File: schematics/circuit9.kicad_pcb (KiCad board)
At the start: 2 copper layers, 47.6 x 31.3 mm, 24 parts, among them J1 Right Pin Strip, J2 Left Pin Strip, J3 Pass-through Output Pin Strip, SW1 SW_DPST_x2, U1 TPS61220DCK, U2 LM321

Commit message: update circuits & order
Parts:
- added JP3: Solder Jumper, Jumper:SolderJumper-2_P1.3mm_Open_RoundedPad1.0x1.5mm, B.Cu at (61.3, 40.0)
- J1: value Right Pin Strip -> Left Pin Strip
- J2: value Left Pin Strip -> Right Pin Strip
- J3: value Pass-through Output Pin Strip -> I/O Pin Strip
- moved C7 9.15 mm to (63.8, 43.7)
- moved R4 6.80 mm to (54.7, 40.4), turned to 180 degrees
- moved R3 2.37 mm to (58.7, 40.4), turned to 180 degrees
- moved C1 2.29 mm to (28.5, 41.9)
- moved C2 2.29 mm to (30.8, 41.9)
- moved U2 1.65 mm to (58.5, 44.7)
- moved R1 0.63 mm to (33.8, 46.7)
- moved R2 0.63 mm to (33.8, 44.6)
- moved C3 0.38 mm to (37.3, 41.7)
- moved C4 0.38 mm to (39.6, 41.7)
- moved C5 0.38 mm to (41.9, 41.7)
- moved C6 0.38 mm to (44.1, 41.7)
- turned C10 to 90 degrees
- turned JP2 to 270 degrees
- renumbered C2 to C1, C1 to C2
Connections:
- C7 pad 1: /V+ -> Net-(C7-Pad1)
- JP2 pad 1: /A7 -> /Vbat
- JP2 pad 2: /Vbat -> /A7
- R3 pad 1: /V+ -> Net-(C7-Pad1)
- U2 pad 5: /V+ -> Net-(C7-Pad1)
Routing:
- net /Vbat: track 16.6 -> 37.3 mm, vias 2 -> 3
- net /GND: track 38.6 -> 18.6 mm, vias 10 -> 12
- net Net-(BT1-Pad1): track 9.16 -> 0.00 mm
- net /V+: track 90.0 -> 85.7 mm, vias 2 -> 4
- net Net-(R3-Pad2): track 9.02 -> 5.55 mm, vias 2 -> 0
- net /Vref: track 22.9 -> 20.7 mm
- net Net-(C7-Pad1): vias 0 -> 2
- added copper zone on B.Cu, net /V+
- added copper zone on B.Cu, net Net-(C7-Pad1)
- added copper zone on F.Cu, net Net-(C7-Pad1)
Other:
- outline, holes or cut-outs redrawn
- board text added: "+: +: R: R: 7: 6: 5: 4: 3: 2: 1: 0:"
- board text added: "Arduino microUSB socket here"
- board text added: "D4: D3: D2:"
- board text added: "D5 GND D6"
- board text added: "Reference Voltage Generator"
- board text added: "close solder jumper to enable reference voltage generator"
- board text added: "close solder jumper to measure battery on A7"
- board text removed: "+ + R R 7 6 5 4 3 2 1 0 D4 D3 D2"
- board text removed: "BRIDGE SOLDER JUMPER TO MEASURE BATTERY CHARGE"
- board text removed: "Left Pin Strip of Arduino Nano 33 BLE Sense"
- board text removed: "Reference Voltage Genreator"
- board text removed: "Right Pin Strip of Arduino"
- board text removed: "https://psylink.me/bp3"

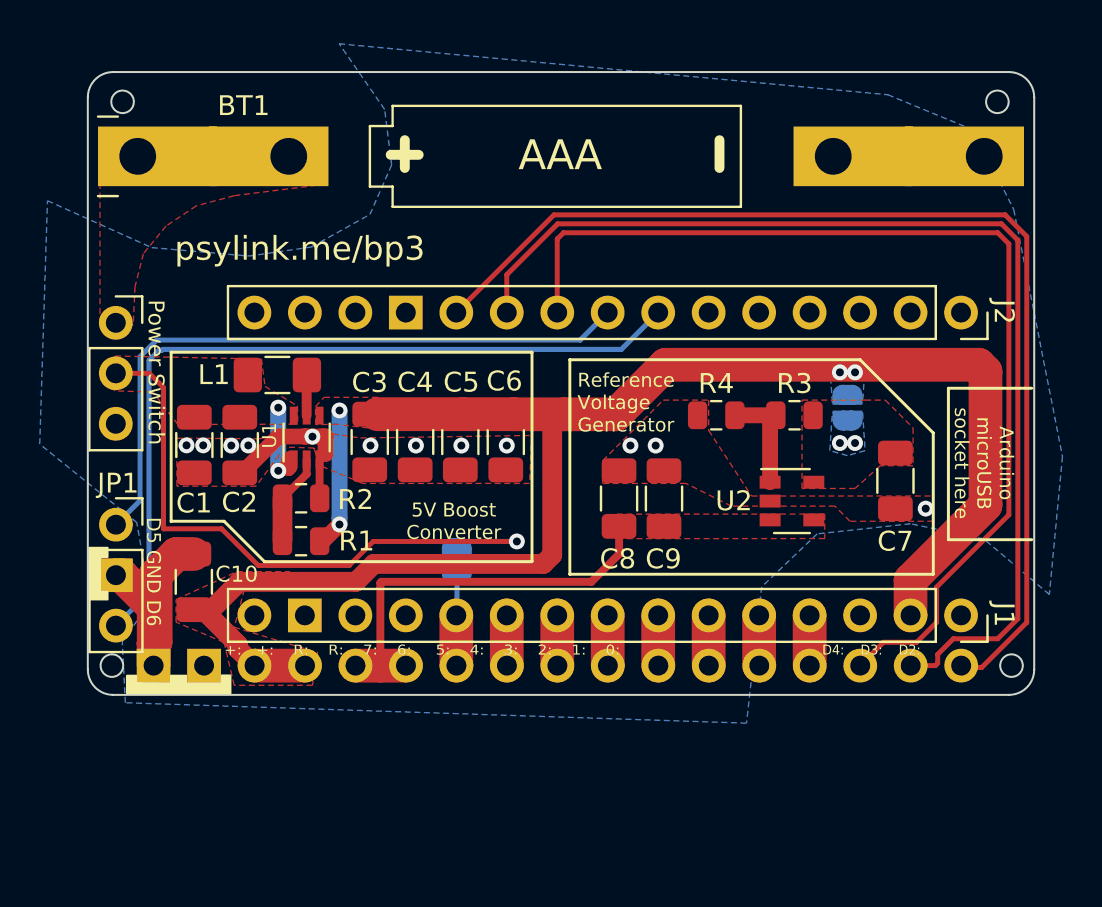
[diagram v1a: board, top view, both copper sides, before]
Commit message: fix bugs in circuit9 schematic + pcb
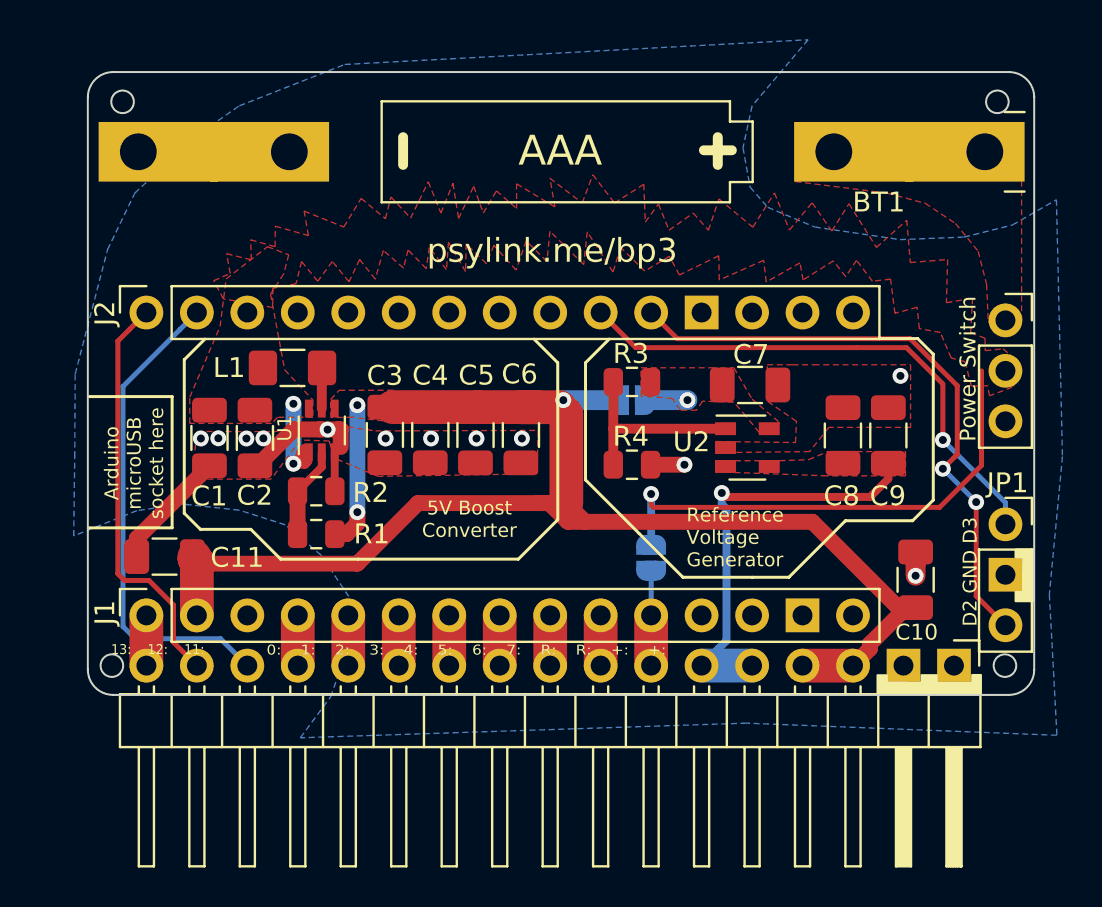
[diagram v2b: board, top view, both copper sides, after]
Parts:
- added C11: 100uF, Capacitor_SMD:C_1206_3216Metric, F.Cu at (27.0, 47.5)
- J3: moved to F.Cu
- SW1: value SW_DPST_x2 -> Power Switch
- moved SW1 44.8 mm to (69.3, 35.6)
- moved JP1 44.8 mm to (69.3, 45.9)
- moved BT1 42.6 mm to (68.3, 27.1), turned to 180 degrees
- moved J1 41.0 mm to (26.1, 50.5), turned to 90 degrees
- moved J2 41.0 mm to (26.1, 35.2), turned to 90 degrees
- moved J3 40.3 mm to (66.7, 53.0)
- moved C10 36.3 mm to (64.8, 48.7)
- moved C9 11.7 mm to (63.4, 41.4)
- moved C8 11.7 mm to (61.1, 41.4)
- moved JP3 10.9 mm to (50.5, 39.6), turned to 0 degrees
- moved JP2 9.78 mm to (51.5, 47.6)
- moved C7 8.76 mm to (56.4, 38.9), turned to 0 degrees
- moved R3 8.35 mm to (50.5, 38.7)
- moved R4 4.92 mm to (50.5, 42.9), turned to 0 degrees
- moved U2 3.50 mm to (56.3, 42.0)
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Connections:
- net Net-(C7-Pad1) renamed /OpAmpV+
- net Net-(L1-Pad2) renamed /L
- net Net-(R1-Pad2) renamed /FB
- net Net-(R3-Pad2) renamed /Vdiv
- J2 pad 3: /D10 -> /Vbat
- J3 pad 15: /D4 -> /D11
- J3 pad 16: /D3 -> /D12
- J3 pad 17: /D2 -> /D13
- JP1 pad 1: /D5 -> /D3
- JP1 pad 3: /D6 -> /D2
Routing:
- net /D4: track 52.1 -> 0.00 mm
- net /D6: track 40.7 -> 0.00 mm
- net /D5: track 33.4 -> 0.11 mm
- net /D3: track 54.7 -> 27.1 mm, vias 0 -> 1
- net /D2: track 55.0 -> 30.6 mm, vias 0 -> 2
- net /D11: track 0.00 -> 24.4 mm
- net /D12: track 0.00 -> 20.7 mm
- net /V+: track 85.7 -> 78.1 mm, vias 4 -> 3
- net /Vbat: track 37.3 -> 30.5 mm
- net /GND: track 18.6 -> 23.8 mm
- net /Vdiv: track 5.55 -> 9.81 mm
- net /D13: track 0.00 -> 2.53 mm
- net /OpAmpV+: track 0.00 -> 2.14 mm, vias 2 -> 1
- net /Vref: track 20.7 -> 21.7 mm, vias 0 -> 1
- removed copper zone on B.Cu, net /OpAmpV+
- removed copper zone on B.Cu, net /V+
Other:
- outline, holes or cut-outs redrawn
- board text added: "0: 1: 2: 3: 4: 5: 6: 7: R: R: +: +:"
- board text added: "13: 12: 11:"
- board text added: "A6 A5 A4 A3 A2 A1 A0"
- board text added: "D11 D12 D13"
- board text added: "D2 GND D3"
- board text removed: "+: +: R: R: 7: 6: 5: 4: 3: 2: 1: 0:"
- board text removed: "D2 D3 D4 A0 A1 A2 A3 A4 A5 A6"
- board text removed: "D4: D3: D2:"
- board text removed: "D5 GND D6"
